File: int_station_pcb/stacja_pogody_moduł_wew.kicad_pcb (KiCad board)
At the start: 2 copper layers, 99.5 x 57 mm, 50 parts, among them J1 10118194-0001LF, J2 USB_C_Receptacle_USB2.0_16P, J3 Conn_01x06, Q1 NPN, Q2 NPN, SW1 SW_Push_Dual_x2, SW2 SW_Push_Dual_x2, SW3 SW_Push_Dual_x2, SW4 SW_Push_Dual_x2, U1 NRF24L01_Breakout, U3 LM39101RS-3.3V, U4 ESP32-WROOM-32E-N4, U5 CH340G, U6 USBLC6-2SC6, U7 USBLC6-2SC6, Y1 Crystal_GND24

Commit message: poprawa plytki wew i zew
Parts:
- removed the C3 at (149.8, 93.2)
- added C12: 22u, Capacitor_Tantalum_SMD:CP_EIA-3528-21_Kemet-B_HandSolder, B.Cu at (154.3, 90.3)
- added C4: 10u, Capacitor_SMD:C_0805_2012Metric_Pad1.18x1.45mm_HandSolder, B.Cu at (154.7, 61.4)
- added C5: 10u, Capacitor_SMD:C_0805_2012Metric_Pad1.18x1.45mm_HandSolder, B.Cu at (156.7, 61.4)
- moved C10 0.51 mm to (165.0, 91.9)
- moved C2 0.38 mm to (152.8, 61.2), turned to -90 degrees
- moved U2 0.36 mm to (158.1, 65.3)
- renumbered C5 to C1, C2 to C10, C9 to C11, C12 to C13, C13 to C14, C4 to C2, C6 to C3, C1 to C6, C10 to C8, C11 to C9, D3 to D2, D2 to D3, J3 to J2, J2 to J3, R4 to R1, R9 to R10, R10 to R12, R14 to R13, R12 to R14, R18 to R15, R13 to R16, R3 to R2, R5 to R3, R6 to R4, R15 to R5, R16 to R6, R17 to R7, R7 to R8, R8 to R9, SW4 to SW3, SW3 to SW4, U6 to U1, U4 to U2, U2 to U3, U7 to U4, U1 to U5, U5 to U6, U3 to U7
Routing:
- net GND: track 14.3 -> 43.4 mm, vias 31 -> 32
- net /ESP_ENABLE: track 223.2 -> 213.3 mm
- net /LCD_MISO: track 127.5 -> 135.8 mm
- net /V_3.3_OUT: track 238.8 -> 244.1 mm
- net /LCD_SCK: track 122.2 -> 125.7 mm
- net /ESP_BOOT: track 109.5 -> 108.2 mm
- net /LCD_T_IRQ: track 63.8 -> 64.8 mm
- net /V_3.3_IN: track 68.5 -> 69.3 mm

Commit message: powiekszyc sciezki do 0.2mm w wew
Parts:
- added C15: 22p, Capacitor_SMD:C_0603_1608Metric_Pad1.08x0.95mm_HandSolder, F.Cu at (144.4, 70.9)
- added C16: 22p, Capacitor_SMD:C_0603_1608Metric_Pad1.08x0.95mm_HandSolder, F.Cu at (145.3, 64.8)
- added R17: 10M, Resistor_SMD:R_0603_1608Metric, F.Cu at (147.0, 68.5)
- added R18: 10k, Resistor_SMD:R_0603_1608Metric, B.Cu at (121.7, 67.4)
- added Y2: 32768Hz, Crystal:Crystal_DS26_D2.0mm_L6.0mm_Horizontal, F.Cu at (145.4, 67.4)
- J3: footprint wyświetlacz lcd:USB_C_Receptacle_TME -> Connector_USB:USB_C_Receptacle_GCT_USB4105-xx-A_16P_TopMnt_Horizontal
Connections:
- U2 pad 33: unconnected-(U2-IO21-Pad33) -> /LCD_CS
- U2 pad 36: unconnected-(U2-IO22-Pad36) -> /NRF_CSN
- U2 pad 6: unconnected-(U2-IO34-Pad6) -> /NRF_IRQ
- U2 pad 8: /NRF_CSN -> Net-(U2-IO32)
- U2 pad 9: /LCD_CS -> Net-(U2-IO33)
- U5 pad 3: /V_3.3_OUT -> Net-(U5-CE)
- U5 pad 8: unconnected-(U5-IRQ-Pad8) -> /NRF_IRQ
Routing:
- net /NRF_IRQ: track 0.00 -> 36.5 mm
- net /NRF_CSN: track 31.0 -> 57.4 mm, vias 0 -> 1
- net /LCD_CS: track 47.4 -> 68.1 mm, vias 0 -> 2
- net Net-(U2-IO32): track 0.00 -> 6.67 mm
- net Net-(U2-IO33): track 0.00 -> 6.17 mm
- net /V_3.3_OUT: track 244.1 -> 247.2 mm
- net /LCD_SCK: track 125.7 -> 128.7 mm
- net Net-(U5-CE): track 0.00 -> 2.88 mm
- net /LCD_MISO: track 135.8 -> 133.1 mm, vias 2 -> 3
- net GND: track 43.4 -> 45.6 mm, vias 32 -> 51
- net /LCD_T_IRQ: track 64.8 -> 66.4 mm
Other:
- board text added: "DTR"
- board text added: "GND"
- board text added: "RTS"
- board text added: "RX"
- board text added: "TX"

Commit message: dokonczona plytka wew
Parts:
- moved Y1 7.81 mm to (146.1, 109.6)
- moved C9 5.06 mm to (141.2, 108.7), turned to 180 degrees
- moved C8 1.34 mm to (144.4, 105.4), turned to 0 degrees
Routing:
- net /MICRO_USB_D-: track 78.1 -> 65.8 mm, vias 2 -> 1
- net GND: track 45.6 -> 52.8 mm, vias 51 -> 61
- net /MICRO_USB_D+: track 76.4 -> 69.6 mm, vias 1 -> 3
- net Net-(U6-XI): track 11.5 -> 6.25 mm
- net /V_3.3_OUT: track 247.2 -> 243.0 mm
- net /ESP_ENABLE: track 213.3 -> 210.0 mm
- net /CH340_UART-: track 109.3 -> 106.2 mm, vias 5 -> 4
- net Net-(U6-XO): track 17.0 -> 14.3 mm
- net /LCD_MOSI: track 135.9 -> 133.4 mm
- net /CH340_DTR: track 46.4 -> 48.7 mm
- net /LCD_T_IRQ: track 66.4 -> 64.2 mm
- net /LCD_SCK: track 128.7 -> 127.3 mm
- net Net-(J1-D-): track 7.67 -> 8.44 mm
- net /LCD_CS: track 68.1 -> 67.5 mm
- net /CH340_UART+: track 106.6 -> 106.2 mm, vias 4 -> 3
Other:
- board text added: "VCC"

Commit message: skonczona plytka wewnetrzna
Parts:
- moved C6 2.67 mm to (126.5, 63.6), turned to 90 degrees
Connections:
- R18 pad 1: /V_3.3_OUT -> /NRF_CE
- U2 pad 23: /LCD_SD_CS -> unconnected-(U2-IO15-Pad23)
- U2 pad 24: unconnected-(U2-IO2-Pad24) -> /LCD_SD_CS
- U2 pad 28: unconnected-(U2-IO17-Pad28) -> /NRF_CE
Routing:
- net /NRF_CE: track 0.00 -> 55.3 mm, vias 0 -> 1
- net /NRF_CSN: track 57.4 -> 47.6 mm, vias 1 -> 2
- net /ESP_BOOT: track 108.6 -> 106.1 mm
- net GND: track 52.8 -> 51.4 mm, vias 61 -> 65
- net /LCD_MISO: track 132.7 -> 134.1 mm
- net /NRF_IRQ: track 36.4 -> 36.9 mm
- net /V_3.3_OUT: track 243.0 -> 243.4 mm, vias 4 -> 3
- net /LCD_MOSI: vias 2 -> 3
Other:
- board text added: "Stacja pogody - Szymon Dobrowolski"

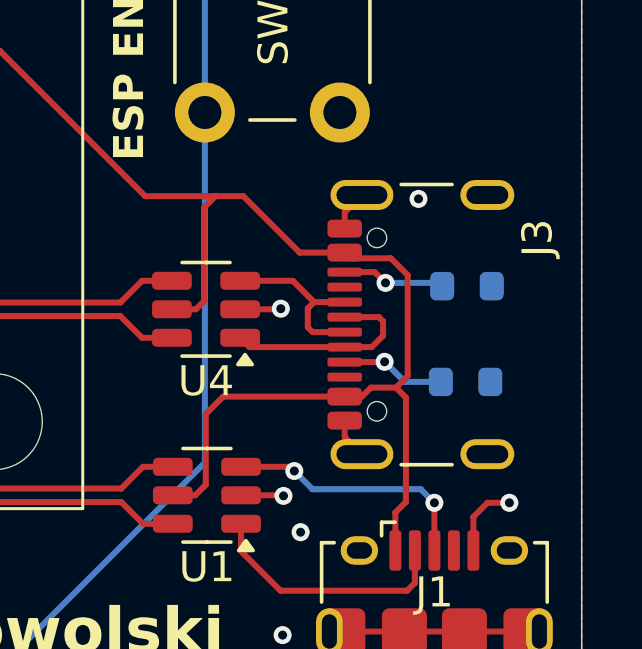
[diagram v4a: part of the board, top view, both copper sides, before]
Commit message: poprawa footprintu usb
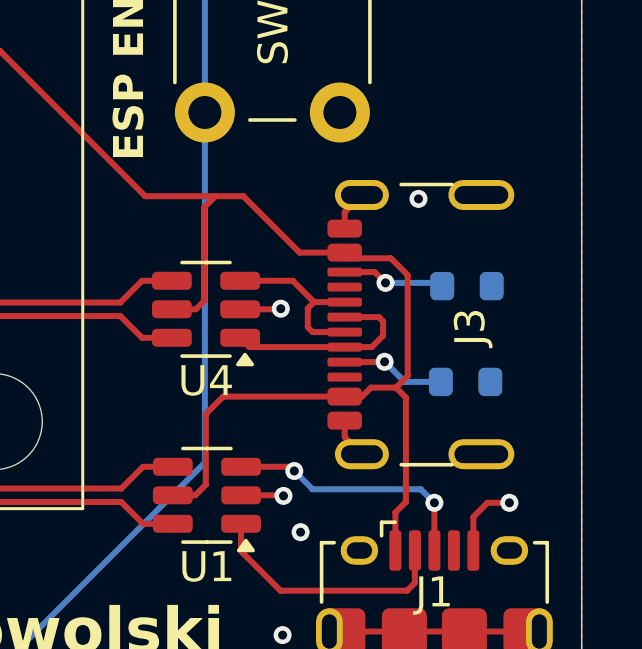
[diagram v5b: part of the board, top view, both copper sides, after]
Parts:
- J3: footprint Connector_USB:USB_C_Receptacle_GCT_USB4105-xx-A_16P_TopMnt_Horizontal -> wyświetlacz lcd:USB_C_Receptacle_TME
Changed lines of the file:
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@@
 		)
 	)
-	(footprint "Connector_USB:USB_C_Receptacle_GCT_USB4105-xx-A_16P_TopMnt_Horizontal"
+	(footprint "wyświetlacz lcd:USB_C_Receptacle_TME"
 		(layer "F.Cu")
 		(at 196.28 103.76 90)
@@
 		(tags "USB C Type-C Receptacle SMD USB 2.0 16P 16C USB4105-15-A USB4105-15-A-060 USB4105-15-A-120 USB4105-GF-A USB4105-GF-A-060 USB4105-GF-A-120")
 		(property "Reference" "J3"
-			(at 2.89 2.75 90)
+			(at -0.07572 0.508928 90)
 			(unlocked yes)
 			(layer "F.SilkS")
@@
 			)
 		)
-		(pad "" np_thru_hole circle
-			(at -2.89 -2.605 90)
-			(size 0.65 0.65)
-			(drill 0.65)
-			(layers "*.Cu" "*.Mask")
-		)
-		(pad "" np_thru_hole circle
-			(at 2.89 -2.605 90)
-			(size 0.65 0.65)
-			(drill 0.65)
-			(layers "*.Cu" "*.Mask")
-		)
 		(pad "A1" smd roundrect
 			(at -3.2 -3.68 90)
@@
 		(pad "S1" thru_hole oval
 			(at -4.32 -3.105 90)
-			(size 1 2.1)
-			(drill oval 0.6 1.7)
-			(property pad_prop_heatsink)
-			(layers "*.Cu" "*.Mask" "F.Paste")
-			(remove_unused_layers no)
-			(net 3 "GND")
-			(pinfunction "SHIELD")
-			(pintype "passive")
-		)
-		(pad "S1" thru_hole oval
-			(at -4.32 1.075 90)
 			(size 1 1.8)
 			(drill oval 0.6 1.4)
@@
 		)
 		(pad "S1" thru_hole oval
-			(at 4.32 -3.105 90)
-			(size 1 2.1)
-			(drill oval 0.6 1.7)
+			(at -4.32 0.875 90)
+			(size 1 2.2)
+			(drill oval 0.6 1.8)
 			(property pad_prop_heatsink)
 			(layers "*.Cu" "*.Mask" "F.Paste")
@@
 		)
 		(pad "S1" thru_hole oval
-			(at 4.32 1.075 90)
+			(at 4.32 -3.105 90)
 			(size 1 1.8)
 			(drill oval 0.6 1.4)
 			(property pad_prop_heatsink)
 			(layers "*.Cu" "*.Mask" "F.Paste")
+			(remove_unused_layers no)
+			(net 3 "GND")
+			(pinfunction "SHIELD")
+			(pintype "passive")
+		)
+		(pad "S1" thru_hole oval
+			(at 4.32 0.875 90)
+			(size 1 2.2)
+			(drill oval 0.6 1.8)
+			(property pad_prop_heatsink)
+			(layers "*.Cu" "*.Mask" "F.Paste")
